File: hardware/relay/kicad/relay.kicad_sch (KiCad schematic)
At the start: 0 parts

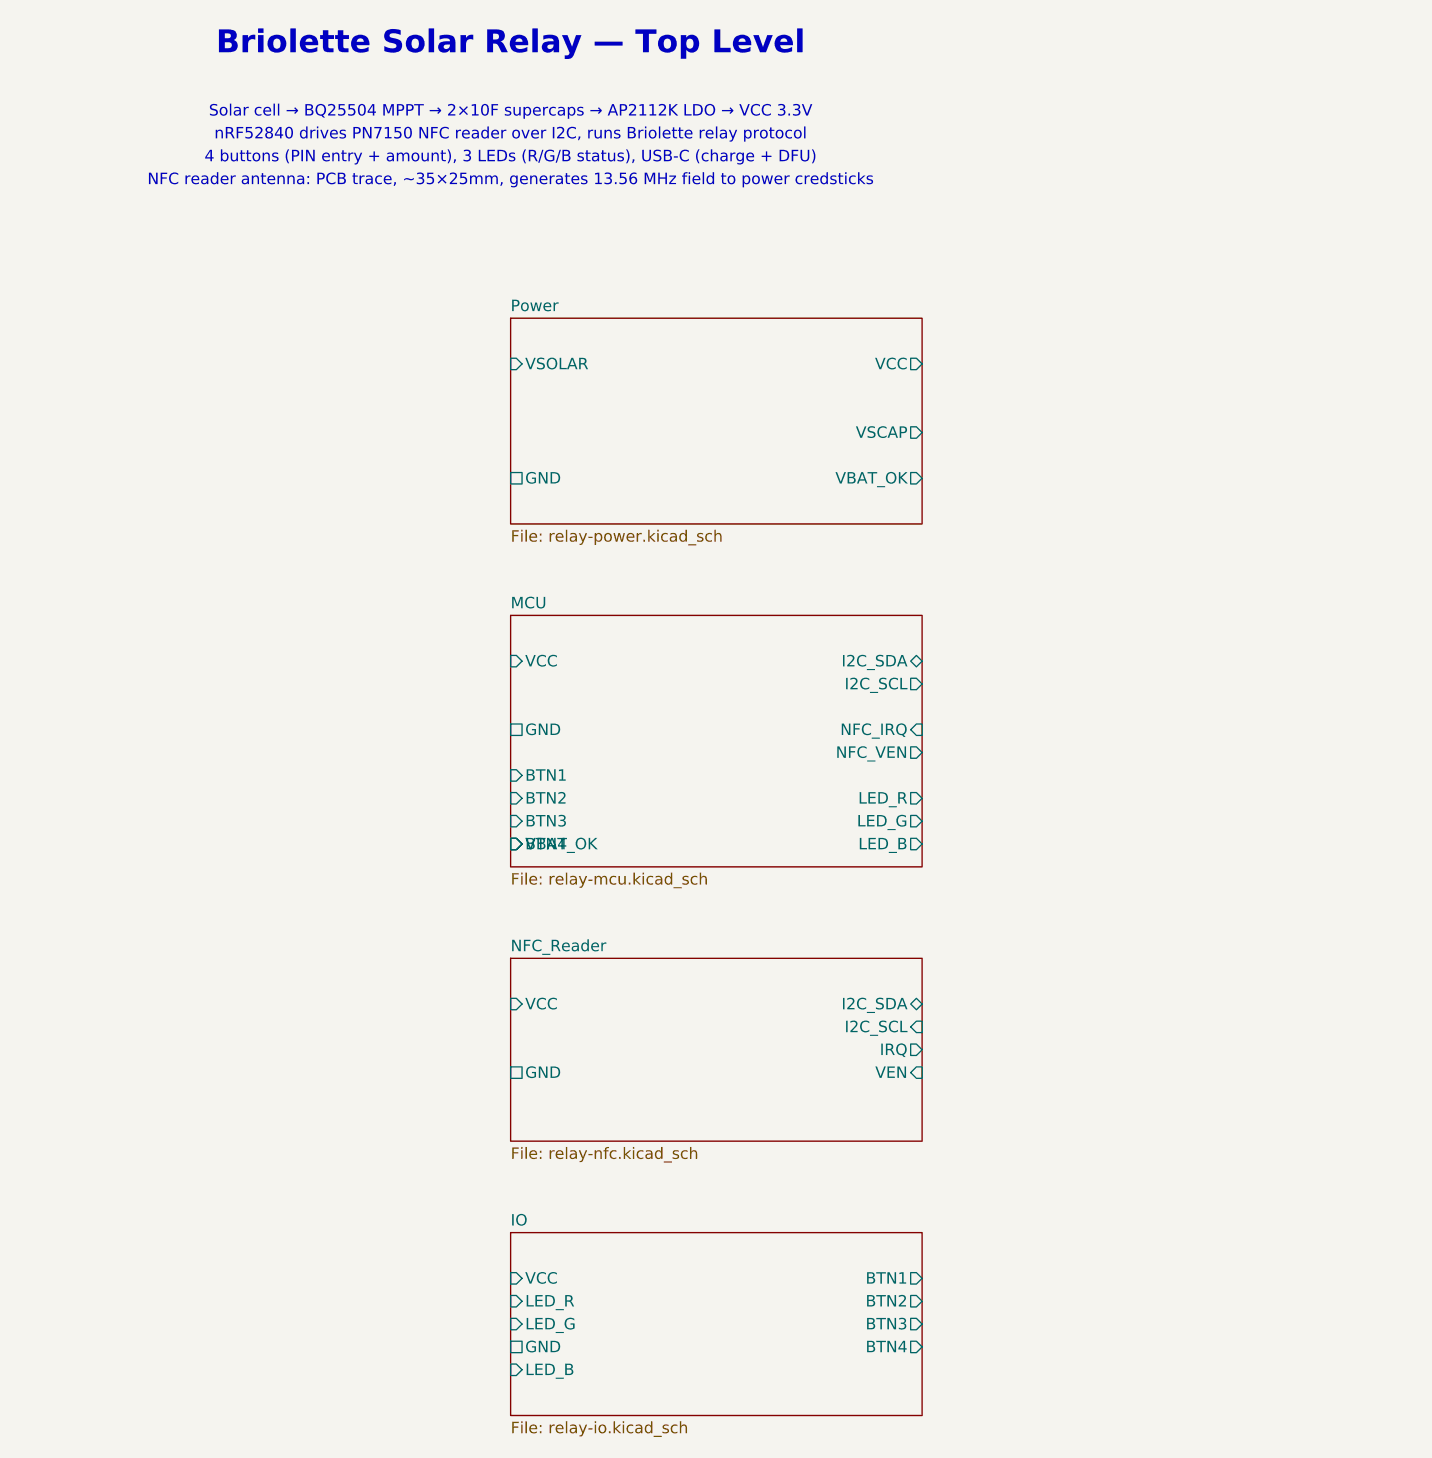
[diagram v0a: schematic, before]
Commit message: Add 13-key numeric keypad to relay using TCA8418 I2C scanner
Replace 4-button vertical column with full numeric keypad for amount
entry (0-9, decimal, OK, Clear). Uses TCA8418 I2C keypad scanner IC
(WQFN-24, 4x4mm, 3µA standby) sharing the existing I2C bus with the
PN7150 NFC controller.

Hardware changes:
- KiCad: TCA8418 symbol + WQFN-24 footprint + 13 switches in 4x4 grid
- PCB: TCA8418 at (-20,-15), switch grid on left side (6mm pitch)
- Schematic: new Keypad sheet, BTN1-4 replaced with KEY_INT/KEY_RST
- Case: 13 button holes in grid pattern (3 empty positions in col 3)
- BOM: +TCA8418RTWR ($0.75), 4→13 switches, +1 decoupling cap

Firmware:
- New briolette-relay-firmware crate with TCA8418 I2C driver
- AmountEntry state machine: digit accumulation, decimal handling,
  OK to confirm (returns cents), Clear to reset
- 6 unit tests passing (matrix mapping, amount entry, display)

Power impact: +3µA idle (negligible vs 12µA existing baseline).

https://claude.ai/code/session_01TM1rFxbipYtvAkh4Vt7My7
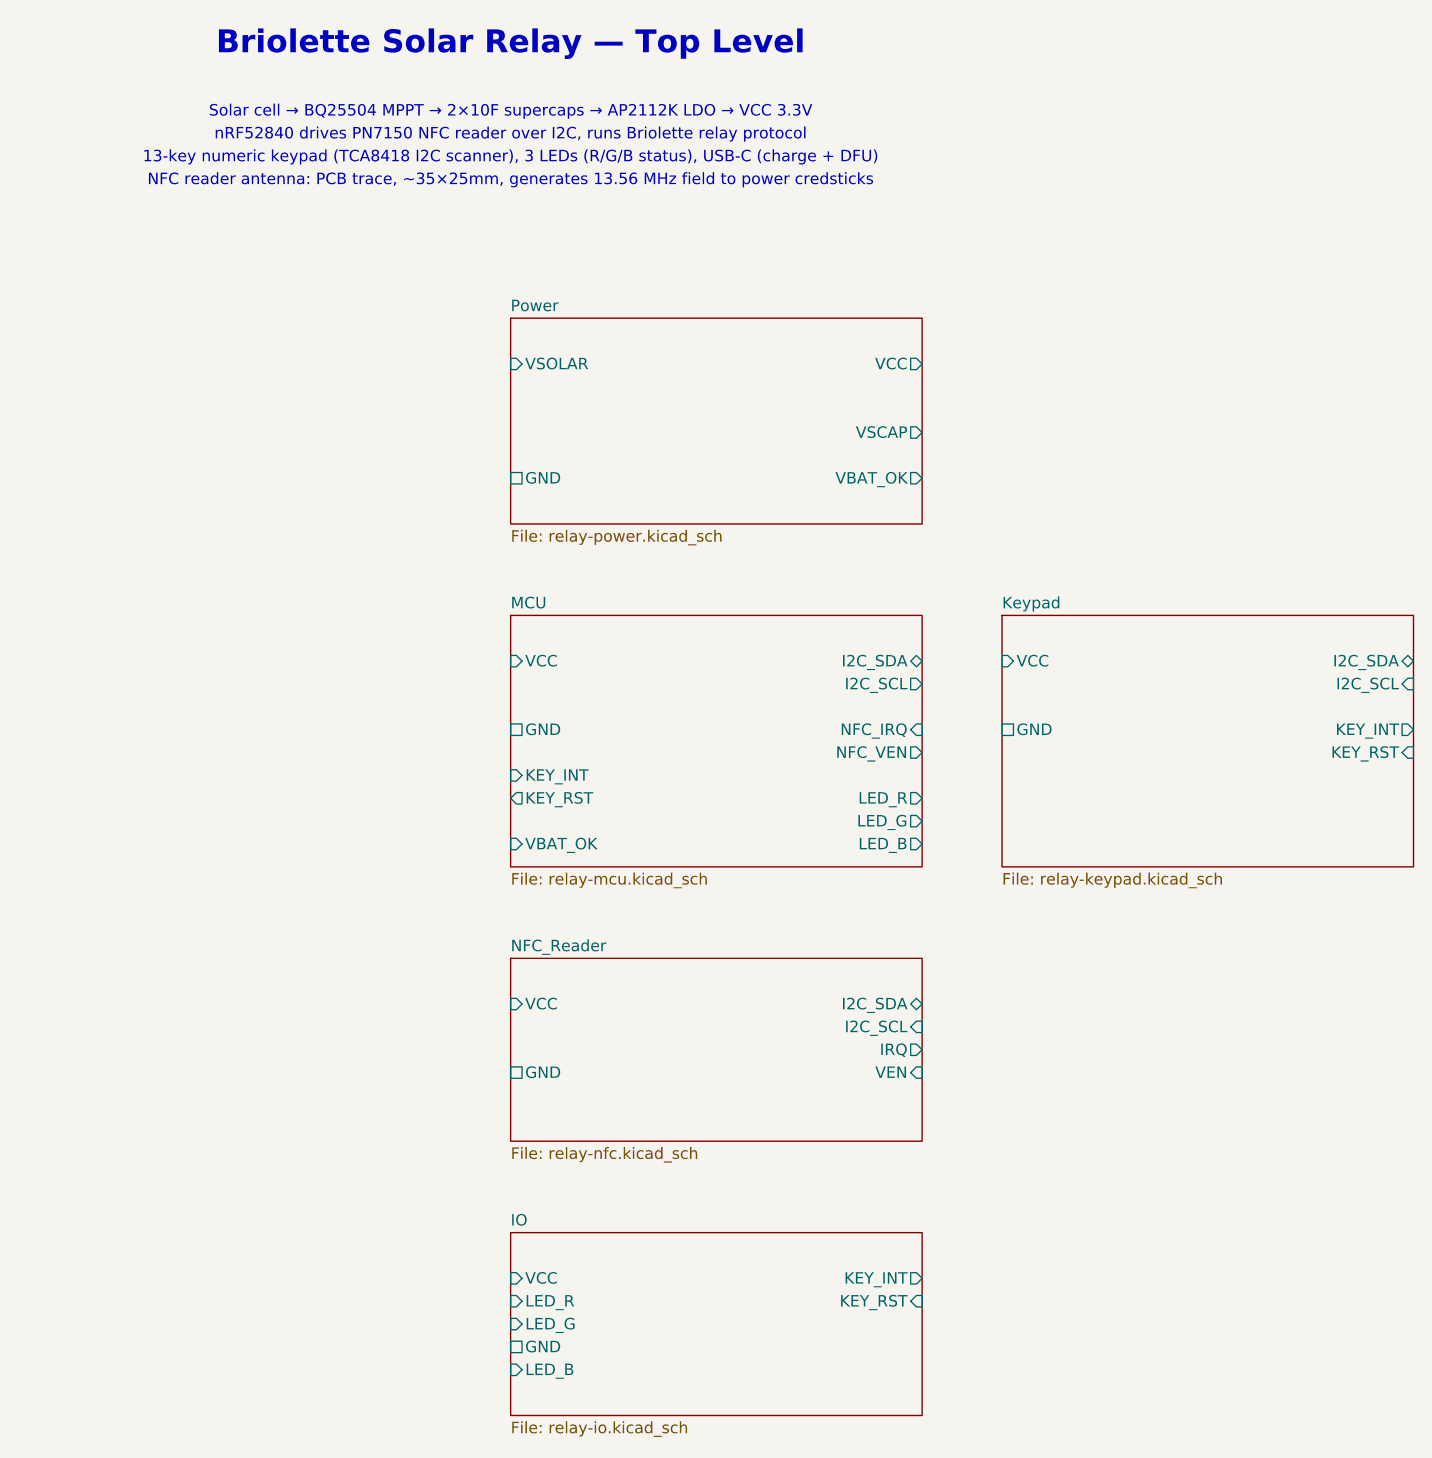
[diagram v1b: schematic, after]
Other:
- added sheet Keypad (relay-keypad.kicad_sch)
- sheet IO ports: added KEY_INT, KEY_RST; removed BTN1, BTN2, BTN3, BTN4
- sheet MCU ports: added KEY_INT, KEY_RST; removed BTN1, BTN2, BTN3, BTN4
- note added: "13-key numeric keypad (TCA8418 I2C scanner), 3 LEDs (R/G/B status), USB-C (charge + DFU)"
- note removed: "4 buttons (PIN entry + amount), 3 LEDs (R/G/B status), USB-C (charge + DFU)"
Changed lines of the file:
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@@
       (effects (font (size 1.27 1.27)) (justify right))
       (uuid "rm-pin-06"))
-    (pin "BTN1" input (at 25.4 101.6 180)
+    (pin "KEY_INT" input (at 25.4 101.6 180)
       (effects (font (size 1.27 1.27)) (justify left))
       (uuid "rm-pin-07"))
-    (pin "BTN2" input (at 25.4 104.14 180)
+    (pin "KEY_RST" output (at 25.4 104.14 180)
       (effects (font (size 1.27 1.27)) (justify left))
       (uuid "rm-pin-08"))
-    (pin "BTN3" input (at 25.4 106.68 180)
-      (effects (font (size 1.27 1.27)) (justify left))
-      (uuid "rm-pin-09"))
-    (pin "BTN4" input (at 25.4 109.22 180)
-      (effects (font (size 1.27 1.27)) (justify left))
-      (uuid "rm-pin-10"))
     (pin "LED_R" output (at 71.12 104.14 0)
       (effects (font (size 1.27 1.27)) (justify right))
@@
   )
   ;; ============================================================
-  ;; Sheet: IO (Buttons, LEDs, USB-C, Piezo)
+  ;; Sheet: Keypad (TCA8418 + 4x4 key matrix)
+  ;; ============================================================
+  (sheet
+    (at 80.0 83.82)
+    (size 45.72 27.94)
+    (stroke (width 0.1524) (type solid))
+    (fill (color 225 255 255 1.0))
+    (property "Sheetname" "Keypad"
+      (at 80.0 83.1846 0)
+      (effects (font (size 1.27 1.27)) (justify left bottom)))
+    (property "Sheetfile" "relay-keypad.kicad_sch"
+      (at 80.0 112.3954 0)
+      (effects (font (size 1.27 1.27)) (justify left top)))
+    (pin "VCC" input (at 80.0 88.9 180)
+      (effects (font (size 1.27 1.27)) (justify left))
+      (uuid "rk-pin-01"))
+    (pin "GND" passive (at 80.0 96.52 180)
+      (effects (font (size 1.27 1.27)) (justify left))
+      (uuid "rk-pin-02"))
+    (pin "I2C_SDA" bidirectional (at 125.72 88.9 0)
+      (effects (font (size 1.27 1.27)) (justify right))
+      (uuid "rk-pin-03"))
+    (pin "I2C_SCL" input (at 125.72 91.44 0)
+      (effects (font (size 1.27 1.27)) (justify right))
+      (uuid "rk-pin-04"))
+    (pin "KEY_INT" output (at 125.72 96.52 0)
+      (effects (font (size 1.27 1.27)) (justify right))
+      (uuid "rk-pin-05"))
+    (pin "KEY_RST" input (at 125.72 99.06 0)
+      (effects (font (size 1.27 1.27)) (justify right))
+      (uuid "rk-pin-06"))
+  )
+  ;; ============================================================
+  ;; Sheet: IO (LEDs, USB-C, Piezo)
   ;; ============================================================
   (sheet
@@
       (effects (font (size 1.27 1.27)) (justify left))
       (uuid "ri-pin-02"))
-    (pin "BTN1" output (at 71.12 157.48 0)
+    (pin "KEY_INT" output (at 71.12 157.48 0)
       (effects (font (size 1.27 1.27)) (justify right))
       (uuid "ri-pin-03"))
-    (pin "BTN2" output (at 71.12 160.02 0)
+    (pin "KEY_RST" input (at 71.12 160.02 0)
       (effects (font (size 1.27 1.27)) (justify right))
       (uuid "ri-pin-04"))
-    (pin "BTN3" output (at 71.12 162.56 0)
-      (effects (font (size 1.27 1.27)) (justify right))
-      (uuid "ri-pin-05"))
-    (pin "BTN4" output (at 71.12 165.1 0)
-      (effects (font (size 1.27 1.27)) (justify right))
-      (uuid "ri-pin-06"))
     (pin "LED_R" input (at 25.4 160.02 180)
       (effects (font (size 1.27 1.27)) (justify left))
@@
     (uuid "txt-relay-0003")
   )
-  (text "4 buttons (PIN entry + amount), 3 LEDs (R/G/B status), USB-C (charge + DFU)"
+  (text "13-key numeric keypad (TCA8418 I2C scanner), 3 LEDs (R/G/B status), USB-C (charge + DFU)"
     (exclude_from_sim no)
     (at 25.4 33.02 0)
